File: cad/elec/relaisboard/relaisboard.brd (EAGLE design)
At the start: 34 x 23 mm, 28 parts, among them IC1 REG1117, T1 MMUN2233

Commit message: increased cleareance here and there
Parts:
- added C14: 2.2u, rcl:C1206
- moved D1 3.91 mm to (7.53, 8.21), turned to 0 degrees
- moved T1 2.42 mm to (11.7, 17.8)
- moved IC1 2.41 mm to (29.5, 16.9)
- moved R3 1.49 mm to (17.2, 17.6)
- moved D5 1.42 mm to (13.8, 9.13)
- moved D6 0.99 mm to (28.2, 19.4)
- moved C45 0.81 mm to (22.9, 19.4)
- moved C1 0.52 mm to (7.19, 4.47)
- moved L1 0.52 mm to (20.2, 8.69)
- moved R5 0.51 mm to (26.9, 8.30)
- moved DZ7 0.46 mm to (26.4, 5.86)
- moved D4 0.42 mm to (16.1, 19.8), turned to 0 degrees
- moved C7 0.38 mm to (26.7, 7.10)
- moved C3 0.25 mm to (14.5, 15.8)
- moved R2 0.25 mm to (15.8, 15.7)
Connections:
- net +3V3: now also C14.1
- net NEUTRAL: now also C14.2
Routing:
- net N$1: track 8.74 -> 1.76 mm
- net +3V3: track 39.1 -> 36.0 mm
- net N$6: track 3.24 -> 5.95 mm
- net NEUTRAL: track 90.4 -> 87.7 mm
- net IO_0: track 25.8 -> 23.8 mm
- net N$9: track 29.6 -> 30.7 mm
- net N$10: track 2.79 -> 1.94 mm
- net +12V: track 41.6 -> 42.3 mm
- net N$2: track 12.5 -> 13.2 mm

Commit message: increased cleareance... again
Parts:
- moved R4 6.74 mm to (21.9, 9.18), flipped to the top, turned to 0 degrees
- moved L1 6.11 mm to (14.1, 9.07)
- moved C7 4.19 mm to (25.7, 3.04)
- moved D5 1.28 mm to (13.4, 10.4), flipped to the top, turned to 180 degrees
- moved R7 1.27 mm to (10.6, 15.3)
- moved R5 1.02 mm to (26.9, 7.28)
- moved R3 0.74 mm to (17.6, 18.2)
- moved C45 0.74 mm to (23.3, 20.0)
- moved D4 0.72 mm to (16.6, 20.3)
- moved U$1 0.68 mm to (20.1, 15.5)
- moved R2 0.65 mm to (15.9, 16.3)
- moved D6 0.51 mm to (28.2, 19.9)
- moved L2 0.51 mm to (12.2, 17.3)
- moved DZ7 0.51 mm to (26.9, 5.86)
- moved D1 0.40 mm to (7.65, 7.83)
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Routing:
- net NEUTRAL: track 87.7 -> 101.9 mm
- net N$2: track 13.2 -> 4.75 mm, vias 1 -> 0
- net N$8: track 3.36 -> 11.1 mm, vias 0 -> 1
- net N$3: track 9.47 -> 15.6 mm
- net IO_0: track 23.8 -> 29.7 mm
- net +3V3: track 36.0 -> 39.3 mm
- net +12V: track 42.3 -> 45.4 mm
- net N$9: track 30.7 -> 28.1 mm, vias 2 -> 3
- net N$11: track 4.69 -> 3.50 mm
- net N$5: track 2.23 -> 2.83 mm

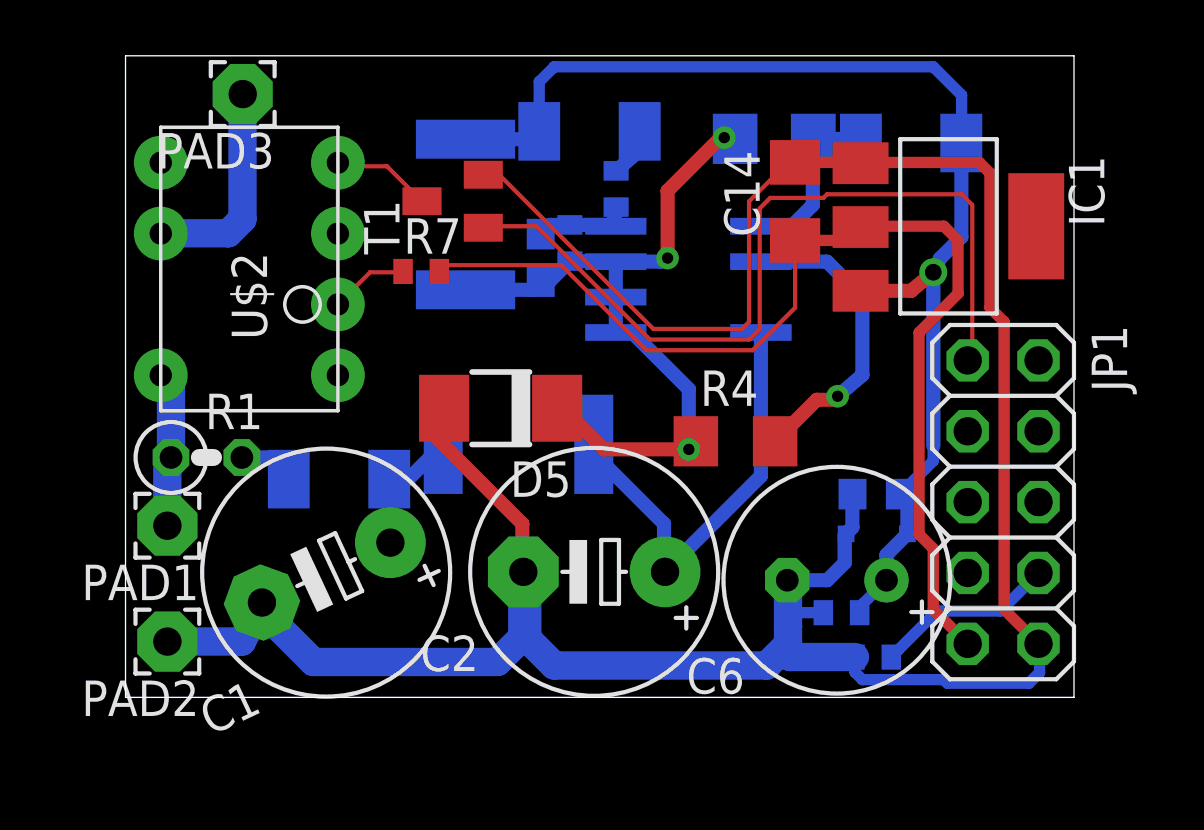
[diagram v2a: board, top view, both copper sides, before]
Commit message: added new battery powered board and changed lots of other stuff
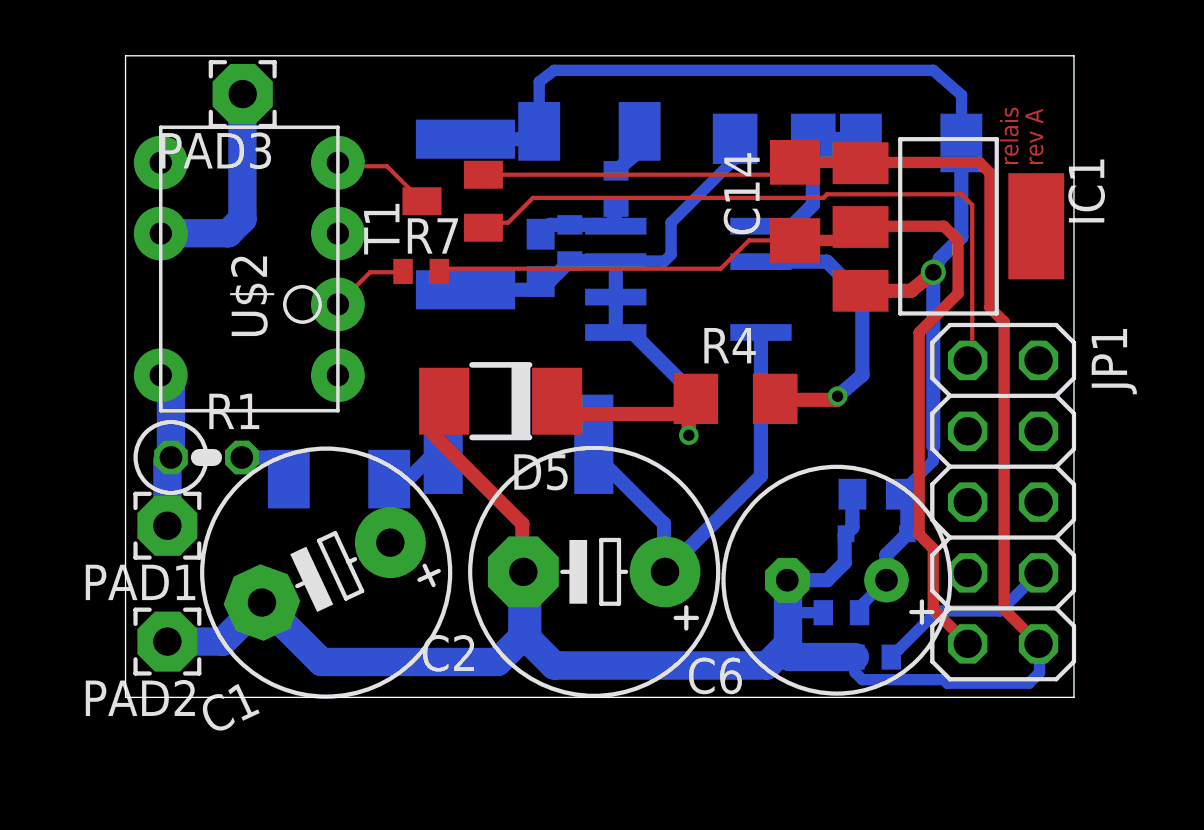
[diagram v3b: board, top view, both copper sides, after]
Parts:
- moved R4 1.52 mm to (21.9, 10.7)
- moved D5 0.25 mm to (13.4, 10.6)
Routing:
- net NEUTRAL: track 101.9 -> 94.9 mm
- net IO_0: track 29.7 -> 23.9 mm
- net +3V3: track 39.3 -> 35.2 mm
- net N$8: track 11.1 -> 10.5 mm
- net N$9: vias 3 -> 1
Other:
- board text added: "FEMALE BOTTOM"
- board text added: "relais"
- board text added: "rev A"
